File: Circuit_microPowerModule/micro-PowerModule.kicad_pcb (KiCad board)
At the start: 2 copper layers, 182.4 x 123.4 mm, 222 parts, among them J101 Screw_Terminal_01x02, J102 Jack-DC, J201 USB_C_Receptacle_USB2.0, J202 Debug, J401 Conn_01x03, J402 Screw_Terminal_01x02, J403 Screw_Terminal_01x02, J404 Screw_Terminal_01x02, J501 Conn_01x05_Pin, J502 MikroBus, Q301 MMBT3906, Q302 RK7002BM, Q303 IRF5305S, Q401 RU1C002ZP, Q402 RK7002BM, Q403 RU1C002ZP, Q404 RK7002BM, Q501 S8550, SW201 KMR2, SW301 SW_DPDT_x2, SW501 RotaryEncoder_Switch, U201 W25Q128JVS, U202 RP2040, U301 OPA376xxDBV, U302 MP2315S, U401 MP2315S, U402 MCP4725xxx-xCH, U403 MT3608, U404 OPA376xxDBV, U405 MCP4725xxx-xCH, U406 INA219BxD, U407 L298N, U408 OPA376xxDBV, U501 MAX485E, Y201 12MHz

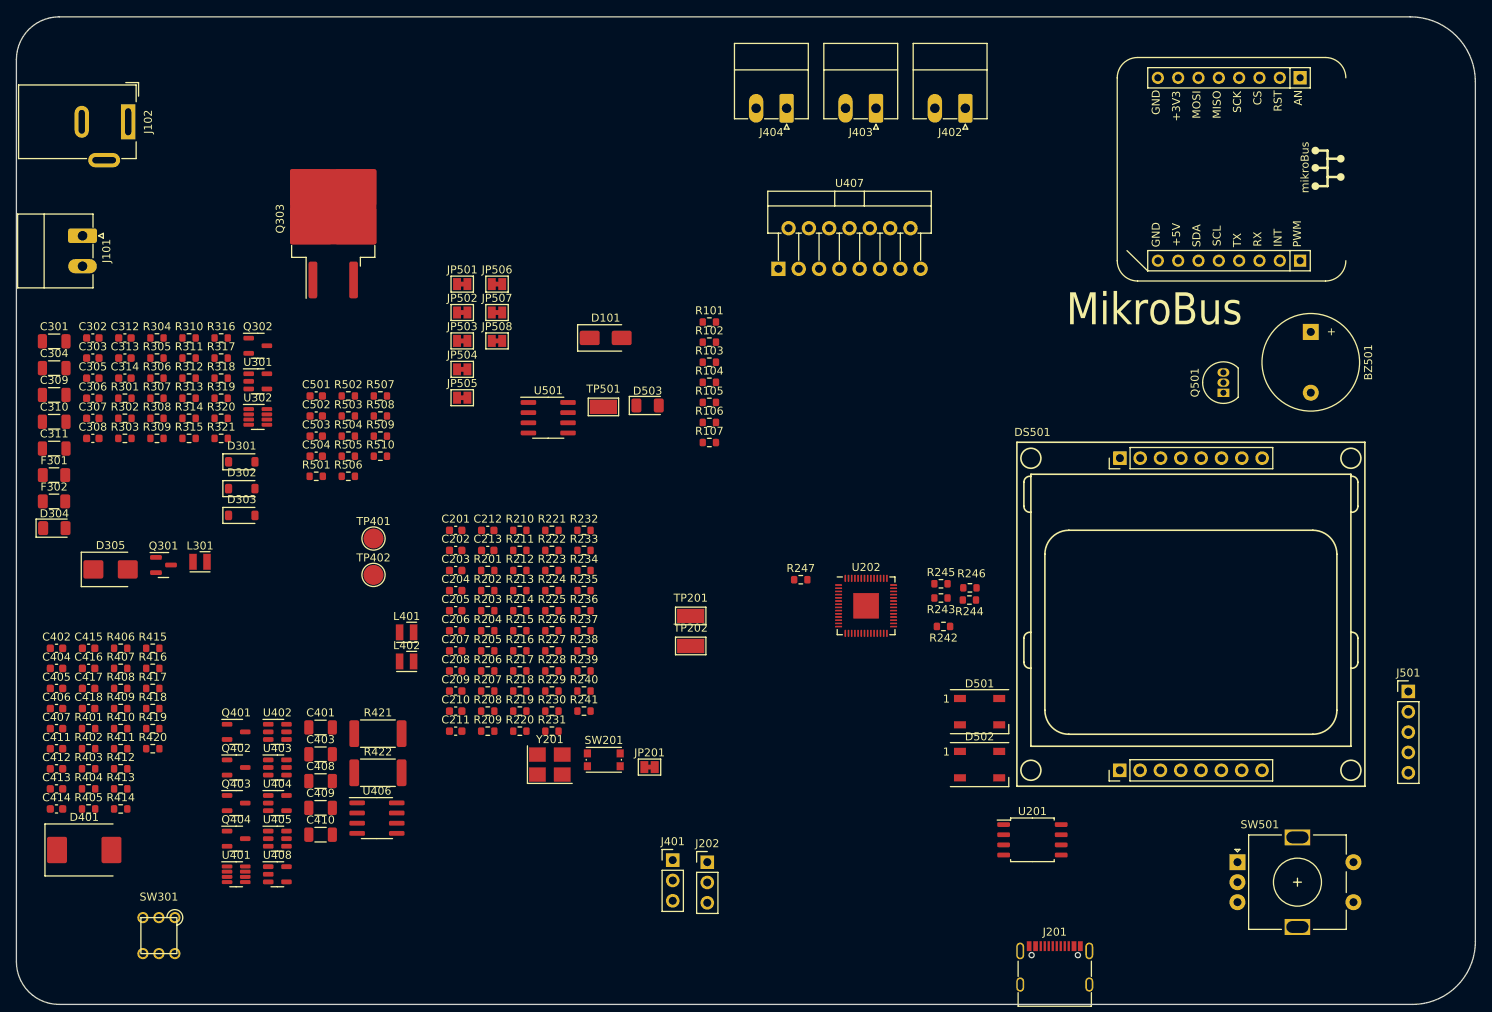
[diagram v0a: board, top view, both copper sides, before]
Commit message: update pcb layout component
target to smaller pcb size
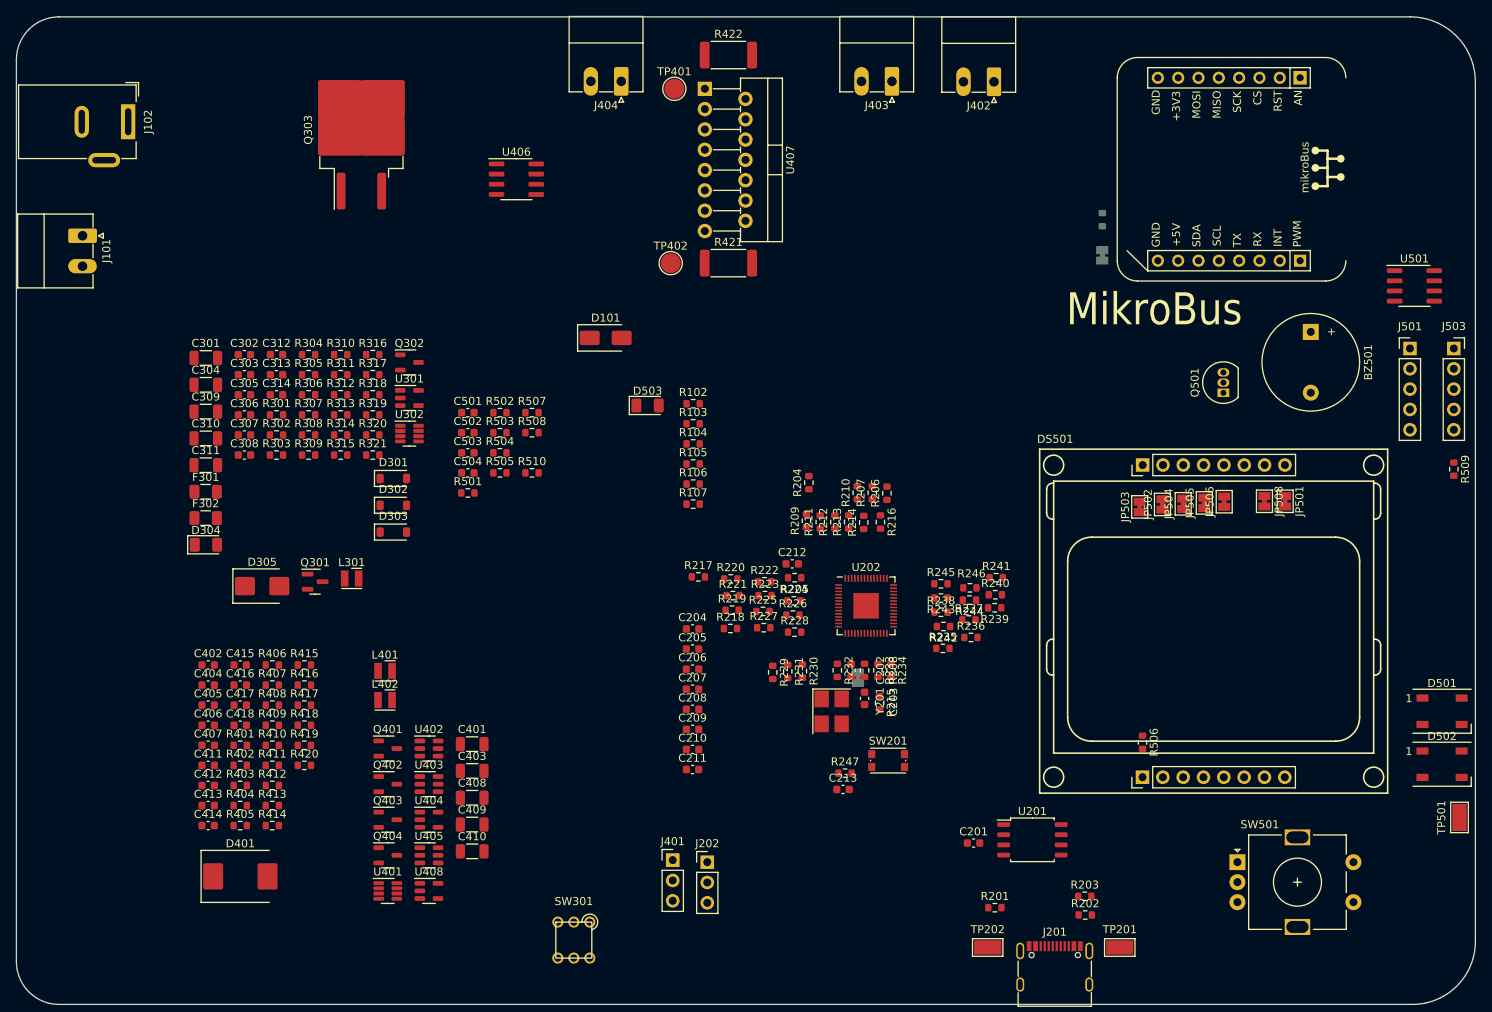
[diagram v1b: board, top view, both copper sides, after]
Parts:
- added J503: HDR-2.54 Female 1x5, Connector_PinSocket_2.54mm:PinSocket_1x05_P2.54mm_Vertical, F.Cu at (204.8, 80.8)
- J501: value Conn_01x05_Pin -> HDR-2.54 Male 1x5
- JP201, JP507, R101: moved to B.Cu
- moved R509 134.2 mm to (204.8, 95.9), turned to -90 degrees
- moved TP501 118.7 mm to (205.5, 139.4), turned to 90 degrees
- moved U501 109.5 mm to (199.9, 73.0)
- moved JP501 106.4 mm to (183.7, 99.9), turned to -90 degrees
- moved R506 104.7 mm to (165.9, 130.0), turned to -90 degrees
- moved R422 99.8 mm to (114.1, 44.1)
- moved JP508 98.0 mm to (181.2, 99.9), turned to -90 degrees
- moved JP506 94.9 mm to (176.1, 100.0), turned to 90 degrees
- moved JP505 93.7 mm to (173.6, 100.1), turned to 90 degrees
- moved JP504 91.7 mm to (171.0, 100.2), turned to 90 degrees
- moved JP502 90.8 mm to (168.4, 100.3), turned to 90 degrees
- moved JP503 87.2 mm to (165.6, 100.6), turned to 90 degrees
- moved R202 85.0 mm to (158.8, 151.6)
- moved R203 82.7 mm to (158.7, 149.3)
- moved U406 81.7 mm to (87.6, 59.7)
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
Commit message: set board edge cut
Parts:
- added C505: 100nF/50V, Capacitor_SMD:C_0603_1608Metric, F.Cu at (197.9, 132.6)
- added C506: 100nF/50V, Capacitor_SMD:C_0603_1608Metric, F.Cu at (197.9, 126.2)
- added REF1: MountingHole_3.2mm_M3_ISO7380, MountingHole:MountingHole_3.2mm_M3_ISO7380, F.Cu at (55.0, 45.5)
- added REF1: MountingHole_3.2mm_M3_ISO7380, MountingHole:MountingHole_3.2mm_M3_ISO7380, F.Cu at (55.0, 155.0)
- added REF1: MountingHole_3.2mm_M3_ISO7380, MountingHole:MountingHole_3.2mm_M3_ISO7380, F.Cu at (95.0, 155.0)
- added REF1: MountingHole_3.2mm_M3_ISO7380, MountingHole:MountingHole_3.2mm_M3_ISO7380, F.Cu at (205.0, 45.2)
- added REF1: MountingHole_3.2mm_M3_ISO7380, MountingHole:MountingHole_3.2mm_M3_ISO7380, F.Cu at (205.2, 157.3)
- C504, JP501, JP502, JP503, JP504, JP505, JP506, JP508, R102, R103, R304, R506: moved to B.Cu
- moved D401 180.9 mm to (233.8, 138.9)
- moved C304 180.9 mm to (229.5, 77.5)
- moved C309 180.9 mm to (229.5, 80.8)
- moved C310 180.9 mm to (229.5, 84.2)
- moved C311 180.9 mm to (229.5, 87.5)
- moved C402 180.9 mm to (229.8, 112.5)
- moved C404 180.9 mm to (229.8, 115.0)
- moved C405 180.9 mm to (229.8, 117.5)
- moved C406 180.9 mm to (229.8, 120.0)
- moved C407 180.9 mm to (229.8, 122.5)
- moved C409 180.9 mm to (262.8, 132.5)
- moved C411 180.9 mm to (229.8, 125.1)
- moved C412 180.9 mm to (229.8, 127.6)
- moved C413 180.9 mm to (229.8, 130.1)
- moved C414 180.9 mm to (229.8, 132.6)
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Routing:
- net /peripheral/DS_Clock: track 0.00 -> 4.54 mm
- net /peripheral/DS_Serial_Data: track 0.00 -> 4.34 mm
- net /peripheral/DS_Data/Command: track 0.00 -> 4.13 mm
- net /peripheral/DS_Backlight: track 0.00 -> 4.07 mm
- net /peripheral/DS_~{Reset}: track 0.00 -> 4.03 mm
- net /peripheral/DS_ChipEnable: track 0.00 -> 3.93 mm
- net GNDREF: track 0.00 -> 3.89 mm
- net Net-(DS501-VCC-Pad1a): track 0.00 -> 3.37 mm
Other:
- board size 182.4 x 123.4 mm -> 163.7 x 124.2 mm

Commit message: Finishing MCU Peripheral Passive Components
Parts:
- added U204: USBLC6-2P6, Package_TO_SOT_SMD:SOT-666, F.Cu at (154.5, 150.5)
- C204, C205, C206, C207, C208, C209, C210, C211: moved to B.Cu
- moved F301 147.7 mm to (92.6, 146.3)
- moved F302 127.7 mm to (101.9, 96.2)
- moved J401 103.5 mm to (124.9, 42.8)
- moved SW301 54.8 mm to (54.9, 142.5), turned to 0 degrees
- moved C213 40.4 mm to (93.0, 116.7), turned to -90 degrees
- moved R104 35.3 mm to (145.0, 93.1), turned to -90 degrees
- moved R105 32.8 mm to (142.5, 93.1), turned to -90 degrees
- moved R215 29.5 mm to (103.7, 122.6), turned to 180 degrees
- moved SW201 29.1 mm to (128.2, 160.8)
- moved Q303 29.0 mm to (75.8, 81.5)
- moved R247 28.2 mm to (133.8, 161.6), turned to 180 degrees
- moved C209 27.9 mm to (134.4, 115.5)
- moved R236 27.7 mm to (120.1, 130.2), turned to -90 degrees
- moved C203 27.7 mm to (104.5, 116.8), turned to 0 degrees
- moved Y201 27.6 mm to (102.9, 112.7), turned to 180 degrees
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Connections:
- R206 pad 2: /main_contorl/USB_P -> /main_contorl/USB+
- R207 pad 2: /main_contorl/USB_N -> /main_contorl/USB-

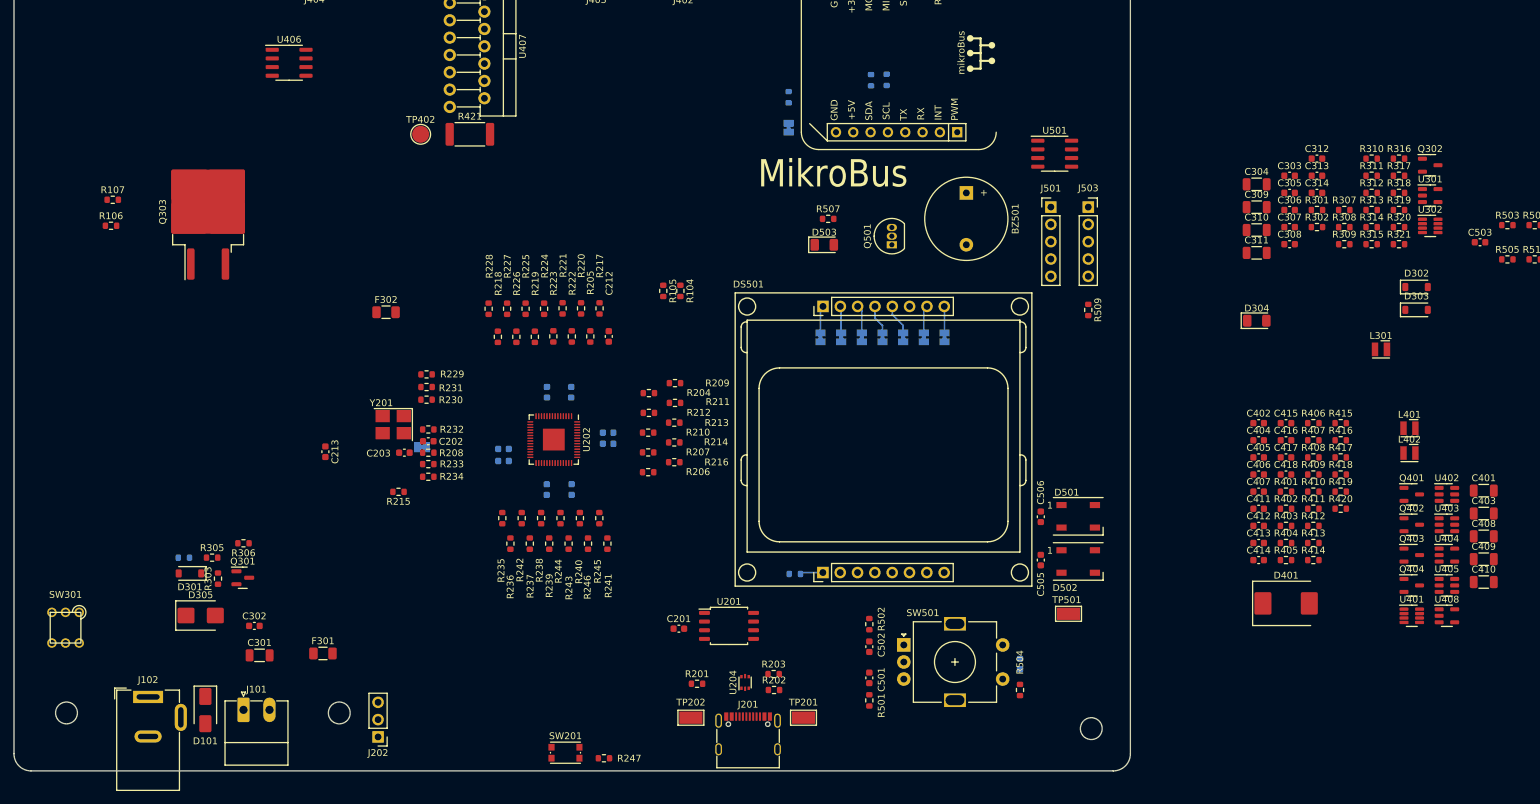
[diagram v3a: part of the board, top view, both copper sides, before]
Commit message: update system power circuit layout
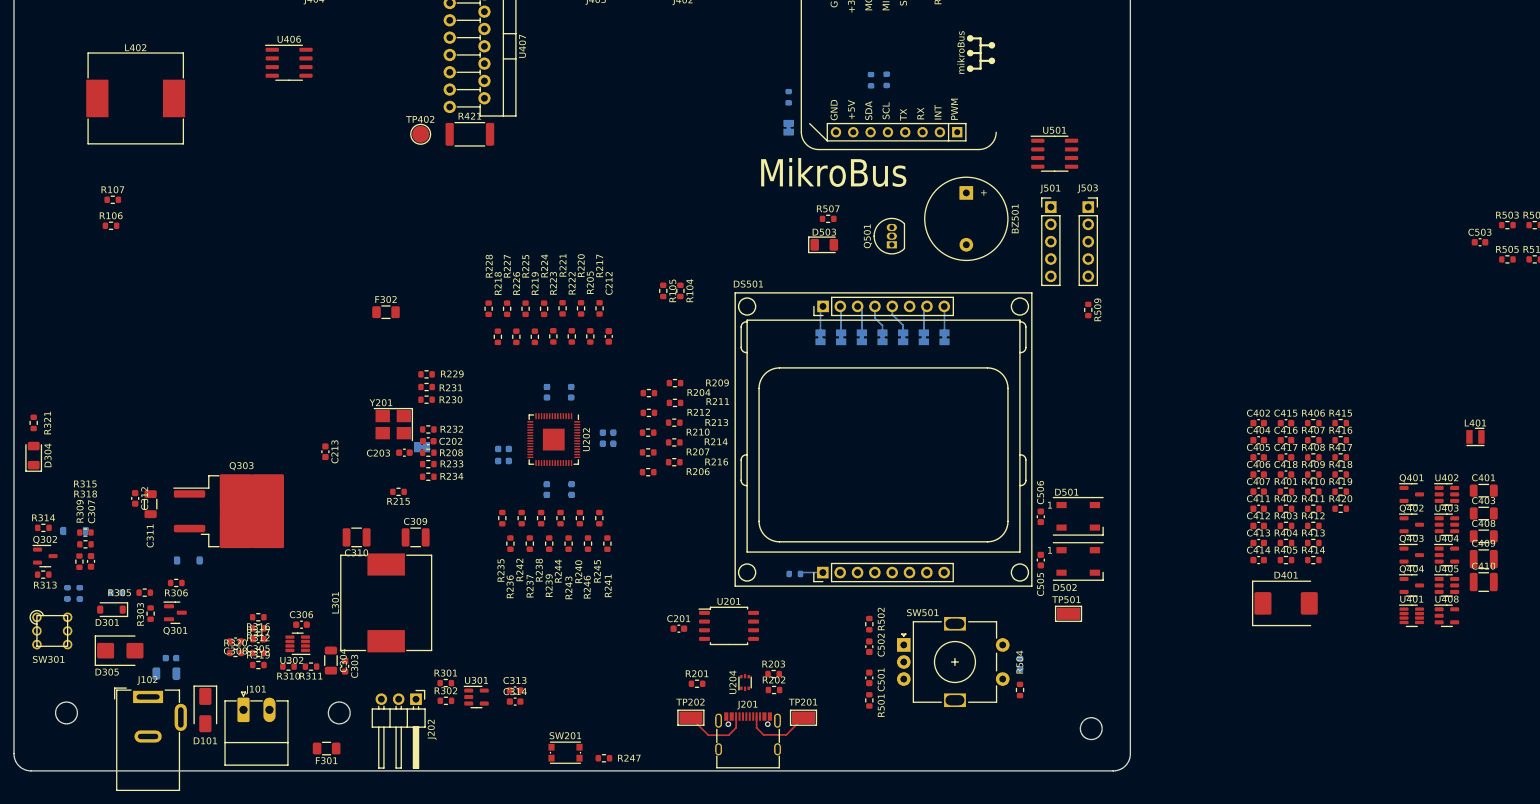
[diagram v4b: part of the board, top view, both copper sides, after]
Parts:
- C301, C302, D302, D303, R307, R308: moved to B.Cu
- C309, C310, C409, C410: footprint Capacitor_SMD:C_1206_3216Metric -> Capacitor_SMD:C_1210_3225Metric
- J202: footprint Connector_PinHeader_2.54mm:PinHeader_1x03_P2.54mm_Vertical -> Connector_PinHeader_2.54mm:PinHeader_1x03_P2.54mm_Horizontal
- L301, L402: footprint Inductor_SMD_Wurth:L_Wurth_WE-LQSH-2512 -> Inductor_SMD:L_Sunlord_MWSA1204S-4R7
- moved Q302 211.0 mm to (51.9, 132.0)
- moved R313 202.0 mm to (51.6, 134.7), turned to 180 degrees
- moved R321 201.9 mm to (50.2, 112.5), turned to -90 degrees
- moved D302 200.0 mm to (56.2, 128.3), turned to 180 degrees
- moved R314 199.7 mm to (51.6, 127.9)
- moved R318 199.4 mm to (57.8, 130.3)
- moved R307 195.5 mm to (55.1, 137.5), turned to -90 degrees
- moved L402 193.9 mm to (65.2, 64.9)
- moved R315 193.3 mm to (57.8, 128.5), turned to 180 degrees
- moved R308 193.0 mm to (56.9, 137.5), turned to 90 degrees
- moved R309 191.2 mm to (56.9, 132.8), turned to -90 degrees
- moved D303 183.8 mm to (72.9, 132.6)
- moved C307 182.5 mm to (58.6, 132.8), turned to 90 degrees
- moved R320 181.7 mm to (79.8, 146.2)
- moved R317 181.3 mm to (83.1, 146.2)
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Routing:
- net Net-(J201-SBU1): track 0.00 -> 10.00 mm
- net Net-(J201-SBU2): track 0.00 -> 9.79 mm

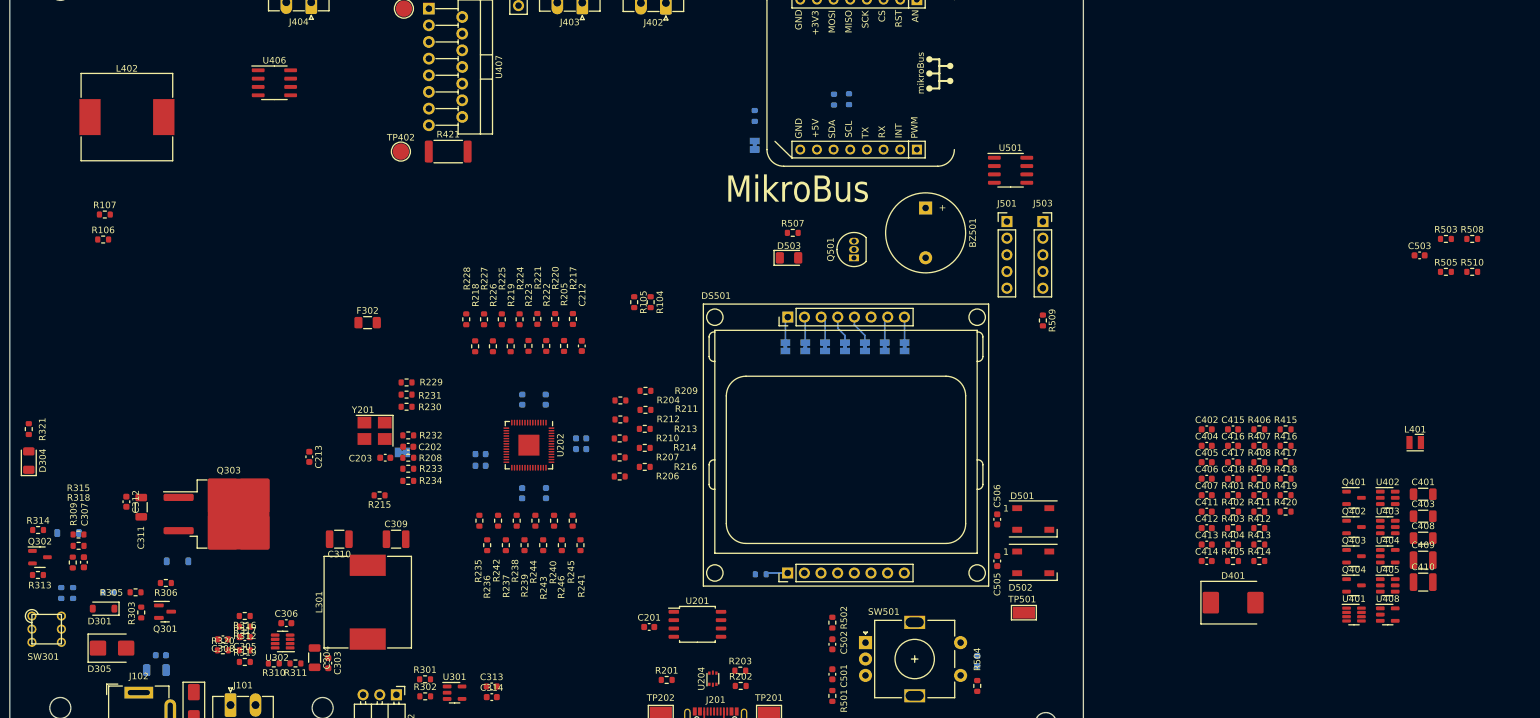
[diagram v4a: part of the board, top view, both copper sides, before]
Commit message: update output inductor footprint
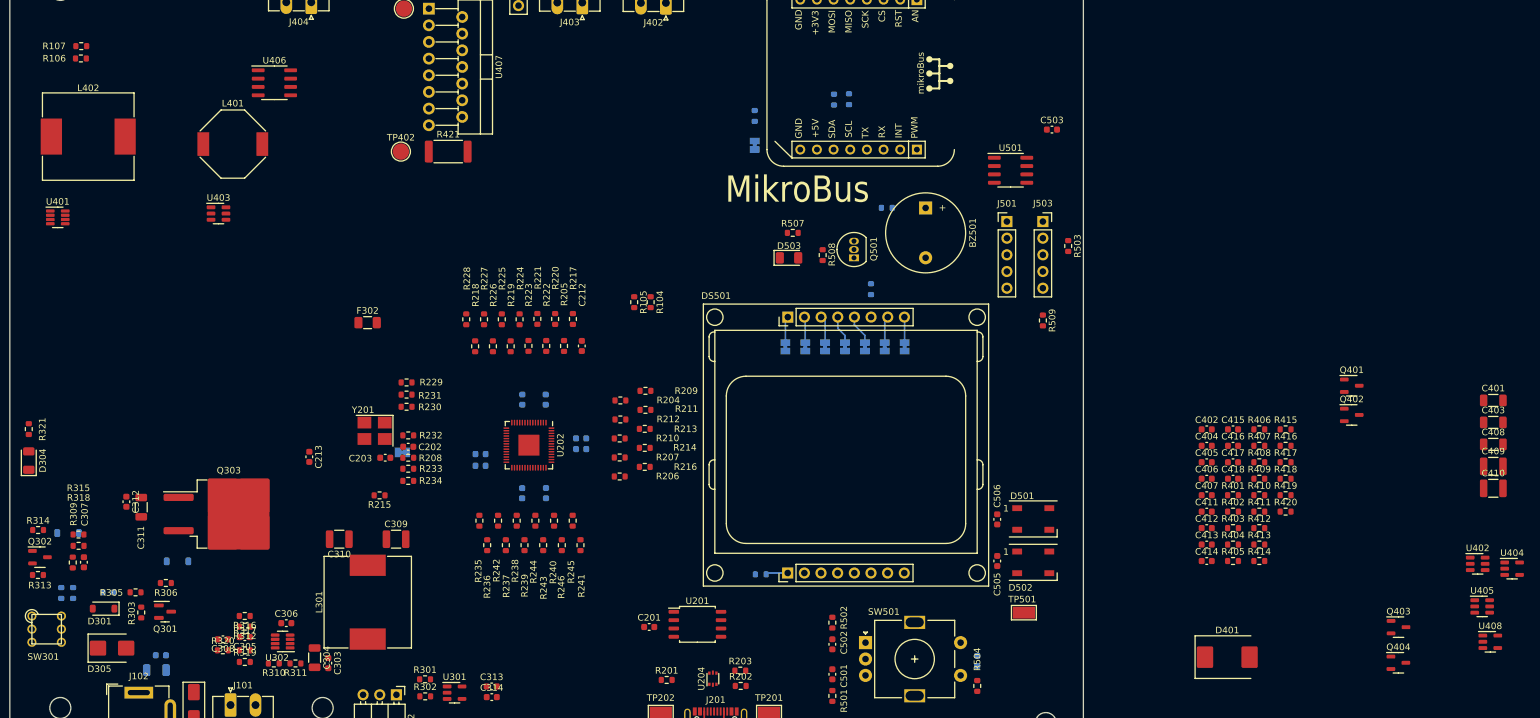
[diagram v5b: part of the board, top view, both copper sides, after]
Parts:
- L401: value 22uH -> 33uH; footprint Inductor_SMD_Wurth:L_Wurth_WE-LQSH-2512 -> Inductor_SMD:L_Bourns-SRU1028_10.0x10.0mm
- R505, R510: moved to B.Cu
- moved U401 206.7 mm to (54.6, 80.2)
- moved L401 185.9 mm to (81.3, 69.0)
- moved U403 184.6 mm to (79.1, 79.6)
- moved R508 99.1 mm to (171.2, 85.9), turned to 90 degrees
- moved R510 89.8 mm to (181.0, 78.7)
- moved R505 87.7 mm to (178.6, 91.1), turned to -90 degrees
- moved C503 59.3 mm to (206.2, 66.8)
- moved R503 57.6 mm to (208.7, 84.6), turned to -90 degrees
- moved R106 27.8 mm to (58.1, 56.0)
- moved R107 25.9 mm to (58.2, 54.1)
- moved U404 19.1 mm to (276.4, 133.8)
- moved C410 17.9 mm to (273.5, 121.5)
- moved C401 17.9 mm to (273.5, 108.1)
- moved C403 17.9 mm to (273.5, 111.5)
- moved C408 17.9 mm to (273.5, 114.8)
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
